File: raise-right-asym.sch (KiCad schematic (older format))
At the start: 105 parts, among them IC1 ATTINY88-A, J1 USB_C_Receptacle_16pin, P1 CONN_01X01, P2 CONN_01X01, P3 CONN_01X01, P4 CONN_01X01, P8 CONN_02X03, Q1 PMOS, -3.6A, 0.02R, SW1 kailh hot plug sockets, SW10 kailh hot plug sockets, SW11 kailh hot plug sockets, SW12 kailh hot plug sockets, SW13 kailh hot plug sockets, SW14 kailh hot plug sockets, SW15 kailh hot plug sockets, SW17 kailh hot plug sockets, SW18 kailh hot plug sockets, SW19 kailh hot plug sockets, SW2 kailh hot plug sockets, SW20 kailh hot plug sockets, SW21 kailh hot plug sockets, SW22 kailh hot plug sockets, SW23 kailh hot plug sockets, SW24 kailh hot plug sockets, SW25 kailh hot plug sockets, SW26 kailh hot plug sockets, SW27 kailh hot plug sockets, SW28 kailh hot plug sockets, SW29 kailh hot plug sockets, SW3 kailh hot plug sockets, SW30 kailh hot plug sockets, SW31 kailh hot plug sockets, SW32 kailh hot plug sockets, SW33 kailh hot plug sockets, SW34 kailh hot plug sockets, SW4 kailh hot plug sockets, SW5 kailh hot plug sockets, SW6 kailh hot plug sockets, SW7 kailh hot plug sockets, SW9 kailh hot plug sockets, T1 CONN_01X01, T2 CONN_01X01, T3 CONN_01X01, U1 ss39et

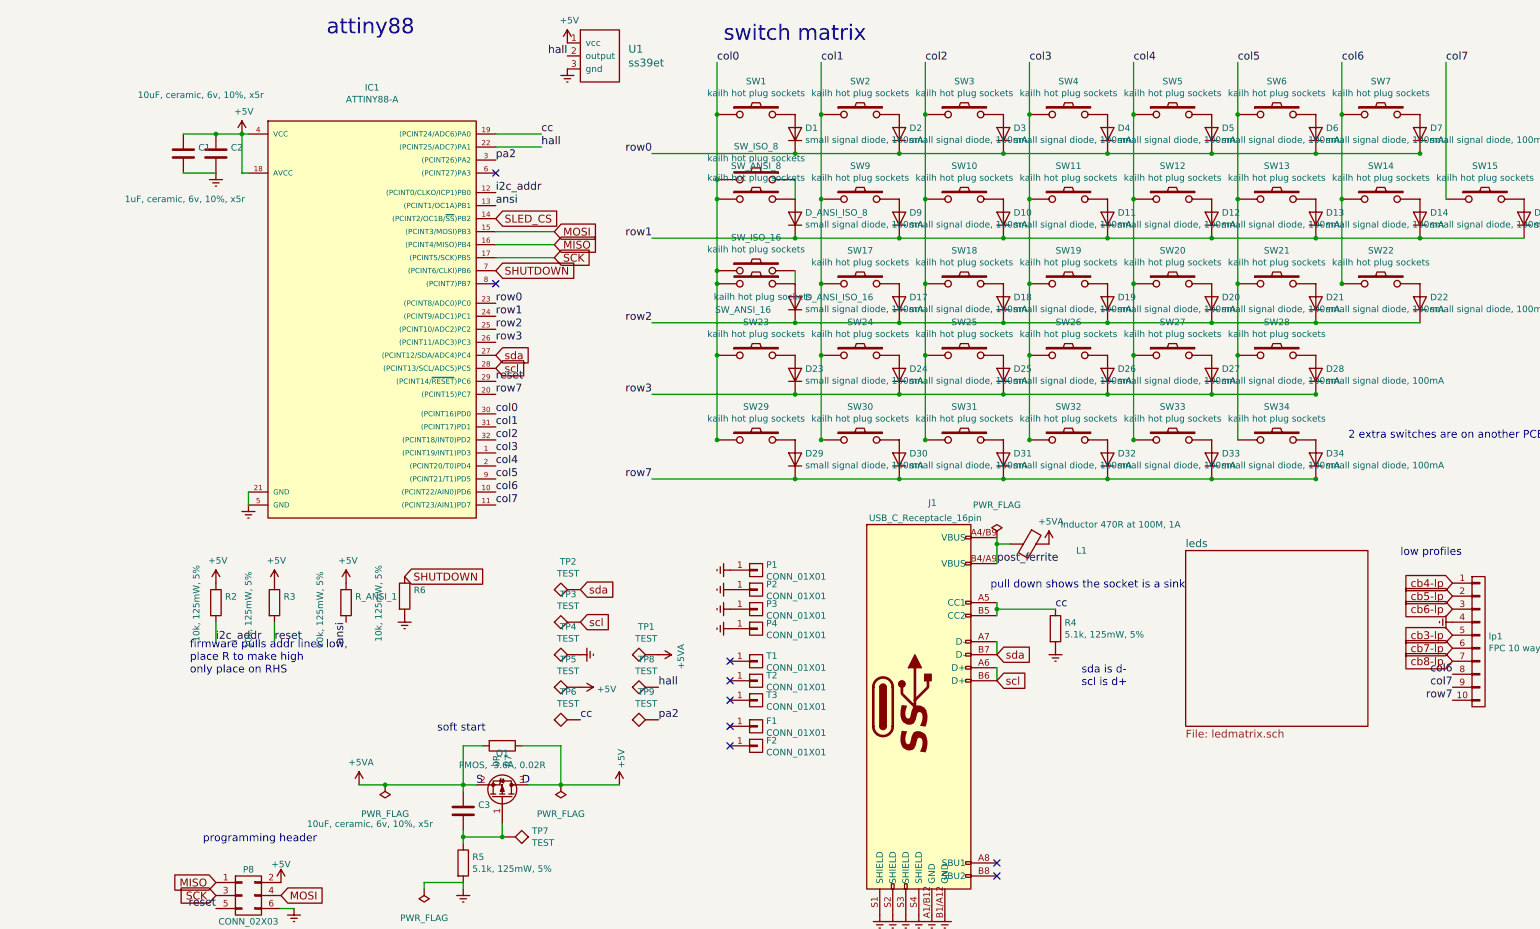
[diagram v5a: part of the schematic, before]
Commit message: 100pf on input, 10uf bypass cap for hall and avcc, testpoints for switches
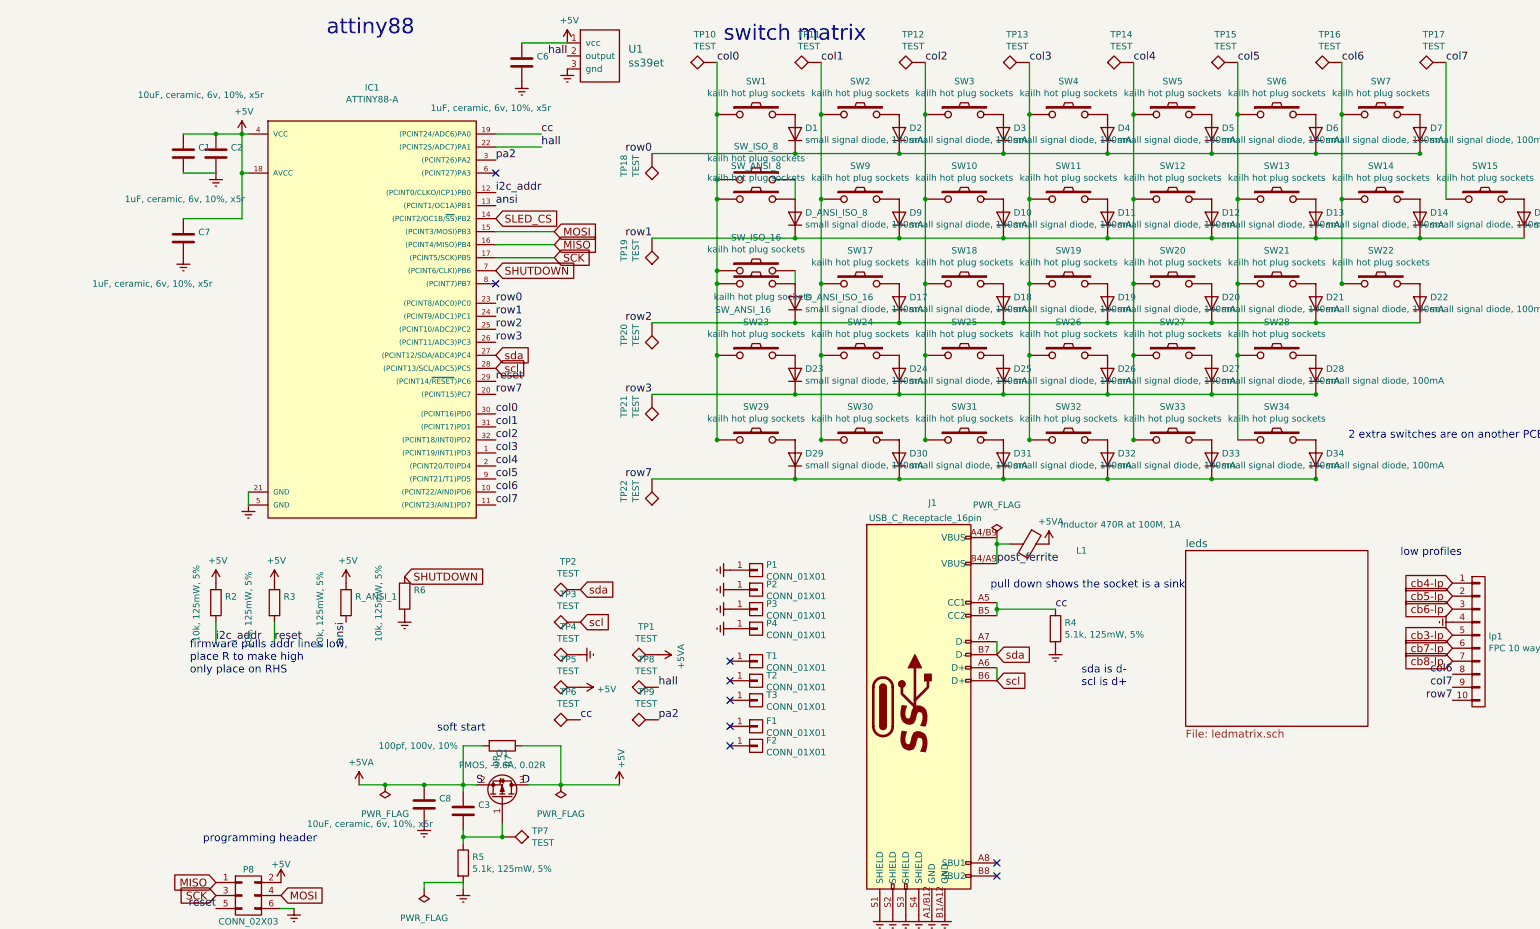
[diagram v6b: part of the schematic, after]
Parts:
- added C6, C7: 1uF, ceramic, 6v, 10%, x5r, raise_fp:C_0603, symbol C
- added C8: 100pf, 100v, 10%, raise_fp:C_0603, symbol C
- added TP10, TP11, TP12, TP13, TP14, TP15, TP16, TP17, TP18, TP19, TP20, TP21, TP22: TEST, raise_fp:Measurement_Point_Round-SMD-Pad_Small, symbol TEST
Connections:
- net +5V: now also C6.1, C7.1
- net +5VA: now also C8.1
- net Earth: now also C6.2, C7.2, C8.2
- net col0: now also TP10.1
- net col1: now also TP11.1
- net col2: now also TP12.1
- net col3: now also TP13.1
- net col4: now also TP14.1
- net col5: now also TP15.1
- net col6: now also TP16.1
- net col7: now also TP17.1
- net row0: now also TP18.1
- net row1: now also TP19.1
- net row2: now also TP20.1
- net row3: now also TP21.1
- net row7: now also TP22.1
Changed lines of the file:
@@
 LIBS:test-jig
 LIBS:usb_c_16pin
-LIBS:Device
 EELAYER 26 0
 EELAYER END
@@
 	1150 1900 1100 1900
 Wire Wire Line
-	1100 1900 1100 1600
+	1100 1600 1100 2250
 Text GLabel 10400 5450 0    60   Input ~ 0
 cb3-lp
+$Comp
+L C C8
+U 1 1 5BEDC1A2
+P 2500 6750
+F 0 "C8" H 2615 6796 50  0000 L CNN
+F 1 "100pf, 100v, 10%" H 2150 7200 50  0000 L CNN
+F 2 "raise_fp:C_0603" H 2538 6600 50  0001 C CNN
+F 3 "" H 2500 6750 50  0000 C CNN
+F 4 "2821263" H 2500 6750 60  0001 C CNN "farnell #"
+F 5 "any/open" H 1850 5000 60  0001 C CNN "supplier"
+F 6 "Value" H 2500 6750 60  0001 C CNN "supplier PN"
+F 7 "Value" H 2500 6750 60  0001 C CNN "MOQ"
+F 8 "Value" H 2500 6750 60  0001 C CNN "leadtime"
+	1    2500 6750
+	1    0    0    -1
+$EndComp
+$Comp
+L Earth #PWR016
+U 1 1 5BEDC459
+P 2500 6900
+F 0 "#PWR016" H 2500 6650 50  0001 C CNN
+F 1 "Earth" H 2500 6750 50  0001 C CNN
+F 2 "" H 2500 6900 50  0000 C CNN
+F 3 "" H 2500 6900 50  0000 C CNN
+	1    2500 6900
+	1    0    0    -1
+$EndComp
+Connection ~ 2500 6600
+$Comp
+L TEST TP22
+U 1 1 5BEDCC0B
+P 4250 4250
+F 0 "TP22" V 4465 4344 50  0000 C CNN
+F 1 "TEST" V 4374 4344 50  0000 C CNN
+F 2 "raise_fp:Measurement_Point_Round-SMD-Pad_Small" H 4250 4250 50  0001 C CNN
+F 3 "" H 4250 4250 50  0001 C CNN
+F 4 "dnp" H 4850 4750 60  0001 C CNN "supplier"
+	1    4250 4250
+	-1   0    0    1
+$EndComp
+$Comp
+L TEST TP21
+U 1 1 5BEDCE9E
+P 4250 3600
+F 0 "TP21" V 4465 3694 50  0000 C CNN
+F 1 "TEST" V 4374 3694 50  0000 C CNN
+F 2 "raise_fp:Measurement_Point_Round-SMD-Pad_Small" H 4250 3600 50  0001 C CNN
+F 3 "" H 4250 3600 50  0001 C CNN
+F 4 "dnp" H 4850 4100 60  0001 C CNN "supplier"
+	1    4250 3600
+	-1   0    0    1
+$EndComp
+$Comp
+L TEST TP20
+U 1 1 5BEDCFA6
+P 4250 3050
+F 0 "TP20" V 4465 3144 50  0000 C CNN
+F 1 "TEST" V 4374 3144 50  0000 C CNN
+F 2 "raise_fp:Measurement_Point_Round-SMD-Pad_Small" H 4250 3050 50  0001 C CNN
+F 3 "" H 4250 3050 50  0001 C CNN
+F 4 "dnp" H 4850 3550 60  0001 C CNN "supplier"
+	1    4250 3050
+	-1   0    0    1
+$EndComp
+$Comp
+L TEST TP19
+U 1 1 5BEDD0A8
+P 4250 2400
+F 0 "TP19" V 4465 2494 50  0000 C CNN
+F 1 "TEST" V 4374 2494 50  0000 C CNN
+F 2 "raise_fp:Measurement_Point_Round-SMD-Pad_Small" H 4250 2400 50  0001 C CNN
+F 3 "" H 4250 2400 50  0001 C CNN
+F 4 "dnp" H 4850 2900 60  0001 C CNN "supplier"
+	1    4250 2400
+	-1   0    0    1
+$EndComp
+$Comp
+L TEST TP18
+U 1 1 5BEDD4B4
+P 4250 1750
+F 0 "TP18" V 4465 1844 50  0000 C CNN
+F 1 "TEST" V 4374 1844 50  0000 C CNN
+F 2 "raise_fp:Measurement_Point_Round-SMD-Pad_Small" H 4250 1750 50  0001 C CNN
+F 3 "" H 4250 1750 50  0001 C CNN
+F 4 "dnp" H 4850 2250 60  0001 C CNN "supplier"
+	1    4250 1750
+	-1   0    0    1
+$EndComp
+$Comp
+L TEST TP10
+U 1 1 5BEDD5BE
+P 4750 1050
+F 0 "TP10" V 4965 1144 50  0000 C CNN
+F 1 "TEST" V 4874 1144 50  0000 C CNN
+F 2 "raise_fp:Measurement_Point_Round-SMD-Pad_Small" H 4750 1050 50  0001 C CNN
+F 3 "" H 4750 1050 50  0001 C CNN
+F 4 "dnp" H 5350 1550 60  0001 C CNN "supplier"
+	1    4750 1050
+	0    -1   -1   0
+$EndComp
+$Comp
+L TEST TP11
+U 1 1 5BEDD76C
+P 5550 1050
+F 0 "TP11" V 5765 1144 50  0000 C CNN
+F 1 "TEST" V 5674 1144 50  0000 C CNN
+F 2 "raise_fp:Measurement_Point_Round-SMD-Pad_Small" H 5550 1050 50  0001 C CNN
+F 3 "" H 5550 1050 50  0001 C CNN
+F 4 "dnp" H 6150 1550 60  0001 C CNN "supplier"
+	1    5550 1050
+	0    -1   -1   0
+$EndComp
+$Comp
+L TEST TP12
+U 1 1 5BEDD884
+P 6350 1050
+F 0 "TP12" V 6565 1144 50  0000 C CNN
+F 1 "TEST" V 6474 1144 50  0000 C CNN
+F 2 "raise_fp:Measurement_Point_Round-SMD-Pad_Small" H 6350 1050 50  0001 C CNN
+F 3 "" H 6350 1050 50  0001 C CNN
+F 4 "dnp" H 6950 1550 60  0001 C CNN "supplier"
+	1    6350 1050
+	0    -1   -1   0
+$EndComp
+$Comp
+L TEST TP13
+U 1 1 5BEDD99E
+P 7150 1050
+F 0 "TP13" V 7365 1144 50  0000 C CNN
+F 1 "TEST" V 7274 1144 50  0000 C CNN
+F 2 "raise_fp:Measurement_Point_Round-SMD-Pad_Small" H 7150 1050 50  0001 C CNN
+F 3 "" H 7150 1050 50  0001 C CNN
+F 4 "dnp" H 7750 1550 60  0001 C CNN "supplier"
+	1    7150 1050
+	0    -1   -1   0
+$EndComp
+$Comp
+L TEST TP14
+U 1 1 5BEDDAB6
+P 7950 1050
+F 0 "TP14" V 8165 1144 50  0000 C CNN
+F 1 "TEST" V 8074 1144 50  0000 C CNN
+F 2 "raise_fp:Measurement_Point_Round-SMD-Pad_Small" H 7950 1050 50  0001 C CNN
+F 3 "" H 7950 1050 50  0001 C CNN
+F 4 "dnp" H 8550 1550 60  0001 C CNN "supplier"
+	1    7950 1050
+	0    -1   -1   0
+$EndComp
+$Comp
+L TEST TP15
+U 1 1 5BEDDFE4
+P 8750 1050
+F 0 "TP15" V 8965 1144 50  0000 C CNN
+F 1 "TEST" V 8874 1144 50  0000 C CNN
+F 2 "raise_fp:Measurement_Point_Round-SMD-Pad_Small" H 8750 1050 50  0001 C CNN
+F 3 "" H 8750 1050 50  0001 C CNN
+F 4 "dnp" H 9350 1550 60  0001 C CNN "supplier"
+	1    8750 1050
+	0    -1   -1   0
+$EndComp
+$Comp
+L TEST TP16
+U 1 1 5BEDE0FE
+P 9550 1050
+F 0 "TP16" V 9765 1144 50  0000 C CNN
+F 1 "TEST" V 9674 1144 50  0000 C CNN
+F 2 "raise_fp:Measurement_Point_Round-SMD-Pad_Small" H 9550 1050 50  0001 C CNN
+F 3 "" H 9550 1050 50  0001 C CNN
+F 4 "dnp" H 10150 1550 60  0001 C CNN "supplier"
+	1    9550 1050
+	0    -1   -1   0
+$EndComp
+$Comp
+L TEST TP17
+U 1 1 5BEDE21E
+P 10350 1050
+F 0 "TP17" V 10565 1144 50  0000 C CNN
+F 1 "TEST" V 10474 1144 50  0000 C CNN
+F 2 "raise_fp:Measurement_Point_Round-SMD-Pad_Small" H 10350 1050 50  0001 C CNN
+F 3 "" H 10350 1050 50  0001 C CNN
+F 4 "dnp" H 10950 1550 60  0001 C CNN "supplier"
+	1    10350 1050
+	0    -1   -1   0
+$EndComp
+$Comp
+L C C7
+U 1 1 5BEDEA06
+P 650 2400
+F 0 "C7" H 765 2446 50  0000 L CNN
+F 1 "1uF, ceramic, 6v, 10%, x5r" H -50 2050 50  0000 L CNN
+F 2 "raise_fp:C_0603" H 688 2250 50  0001 C CNN
+F 3 "" H 650 2400 50  0000 C CNN
+F 4 "1865556" H 650 2400 60  0001 C CNN "farnell #"
+F 5 "any/open" H -250 650 60  0001 C CNN "supplier"
+	1    650  2400
+	1    0    0    -1
+$EndComp
+$Comp
+L Earth #PWR038
+U 1 1 5BEDEB4C
+P 650 2550
+F 0 "#PWR038" H 650 2300 50  0001 C CNN
+F 1 "Earth" H 650 2400 50  0001 C CNN
+F 2 "" H 650 2550 50  0000 C CNN
+F 3 "" H 650 2550 50  0000 C CNN
+	1    650  2550
+	1    0    0    -1
+$EndComp
+Wire Wire Line
+	1100 2250 650  2250
+Connection ~ 1100 1900
+$Comp
+L C C6
+U 1 1 5BEDF086
+P 3250 1050
+F 0 "C6" H 3365 1096 50  0000 L CNN
+F 1 "1uF, ceramic, 6v, 10%, x5r" H 2550 700 50  0000 L CNN
+F 2 "raise_fp:C_0603" H 3288 900 50  0001 C CNN
+F 3 "" H 3250 1050 50  0000 C CNN
+F 4 "1865556" H 3250 1050 60  0001 C CNN "farnell #"
+F 5 "any/open" H 2350 -700 60  0001 C CNN "supplier"
+	1    3250 1050
+	1    0    0    -1
+$EndComp
+$Comp
+L Earth #PWR039
+U 1 1 5BEDF1C2
+P 3250 1200
+F 0 "#PWR039" H 3250 950 50  0001 C CNN
+F 1 "Earth" H 3250 1050 50  0001 C CNN
+F 2 "" H 3250 1200 50  0000 C CNN
+F 3 "" H 3250 1200 50  0000 C CNN
+	1    3250 1200
+	1    0    0    -1
+$EndComp
+Wire Wire Line
+	3250 900  3600 900
 $EndSCHEMATC

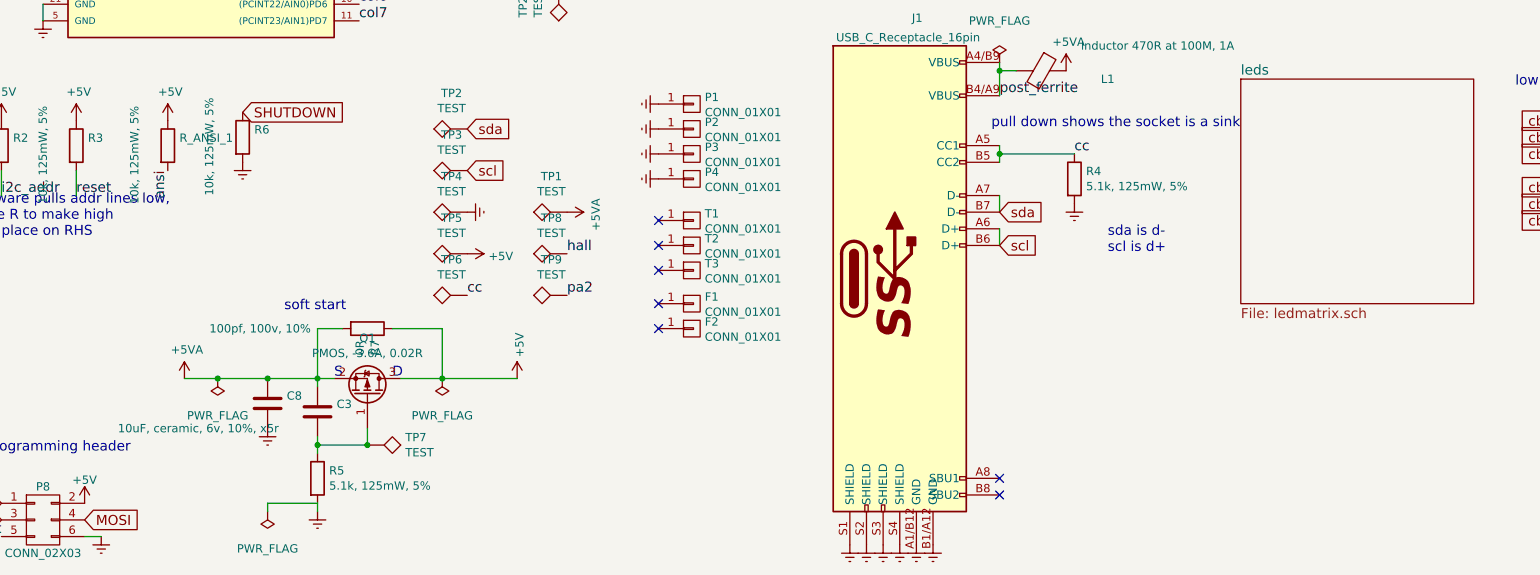
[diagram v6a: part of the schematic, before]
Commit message: holes to 4mm, sled testpoints, usbC mask on locator points, diode and cap fp improvements
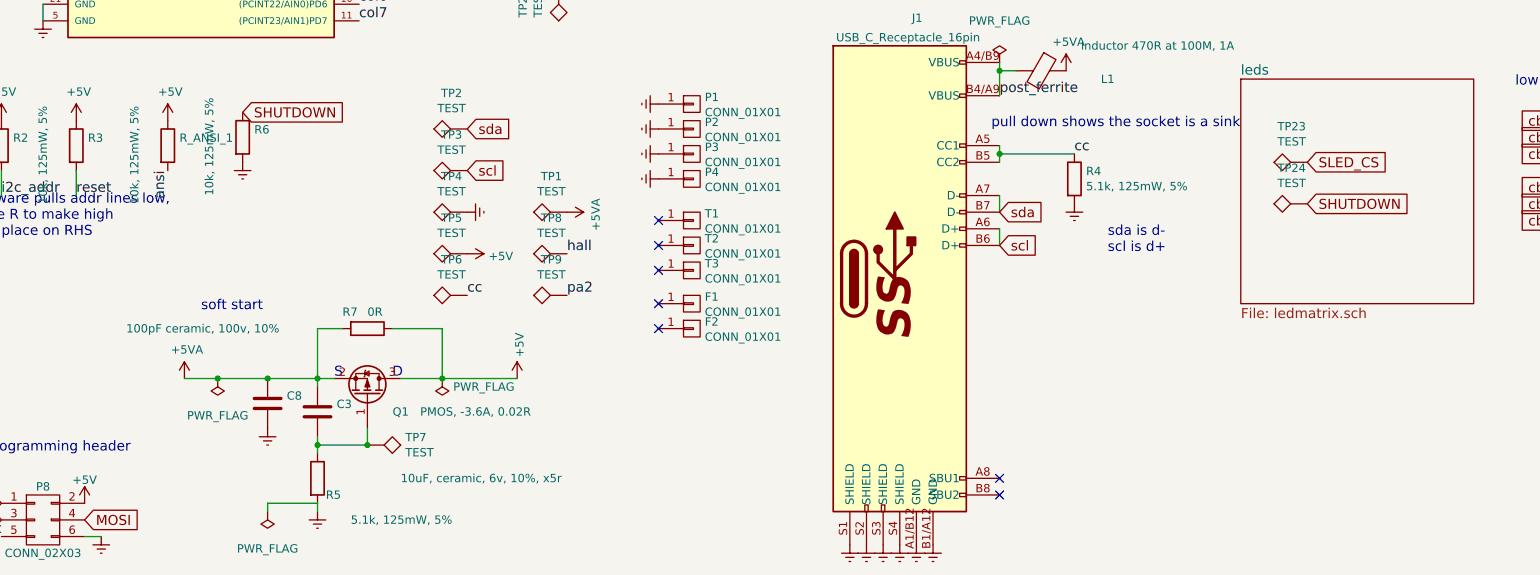
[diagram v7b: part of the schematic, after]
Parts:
- added TP23, TP24: TEST, raise_fp:Measurement_Point_Round-SMD-Pad_Small, symbol TEST
- C8: value 100pf, 100v, 10% -> 100pF ceramic, 100v, 10%
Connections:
- net SHUTDOWN: now also TP24.1
- net SLED_CS: now also TP23.1
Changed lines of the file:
@@
 P 2800 6800
 F 0 "C3" H 2915 6846 50  0000 L CNN
-F 1 "10uF, ceramic, 6v, 10%, x5r" H 1600 6700 50  0000 L CNN
+F 1 "10uF, ceramic, 6v, 10%, x5r" H 3300 6400 50  0000 L CNN
 F 2 "raise_fp:C_0603" H 2838 6650 50  0001 C CNN
 F 3 "" H 2800 6800 50  0000 C CNN
@@
 U 1 1 59D15DC4
 P 2800 7200
-F 0 "R5" H 2870 7246 50  0000 L CNN
-F 1 "5.1k, 125mW, 5%" H 2870 7155 50  0000 L CNN
+F 0 "R5" H 2850 7100 50  0000 L CNN
+F 1 "5.1k, 125mW, 5%" H 3000 6950 50  0000 L CNN
 F 2 "raise_fp:R_0603" V 2730 7200 50  0001 C CNN
 F 3 "" H 2800 7200 50  0000 C CNN
@@
 	1    0    0    -1
 $EndComp
-Text Notes 2600 6200 0    60   ~ 0
+Text Notes 2100 6200 0    60   ~ 0
 soft start
 $Comp
@@
 P 3550 6600
 F 0 "#FLG03" H 3550 6695 50  0001 C CNN
-F 1 "PWR_FLAG" H 3550 6823 50  0000 C CNN
+F 1 "PWR_FLAG" H 3300 6650 50  0000 C CNN
 F 2 "" H 3550 6600 50  0000 C CNN
 F 3 "" H 3550 6600 50  0000 C CNN
@@
 	1    0    0    -1
 $EndComp
-$Sheet
-S 8350 4800 1400 1350
-U 59D12F0F
-F0 "leds" 60
-F1 "ledmatrix.sch" 60
-$EndSheet
 $Comp
 L SW_PUSH SW14
@@
 U 1 1 5A315925
 P 3100 6700
-F 0 "Q1" V 3443 6700 50  0000 C CNN
-F 1 "PMOS, -3.6A, 0.02R" V 3352 6700 50  0000 C CNN
+F 0 "Q1" V 3000 6900 50  0000 C CNN
+F 1 "PMOS, -3.6A, 0.02R" V 3000 7350 50  0000 C CNN
 F 2 "raise_fp:SOT-23" H 3300 6800 50  0001 C CNN
 F 3 "" H 3100 6700 50  0001 C CNN
@@
 U 1 1 5B2B6980
 P 3100 6300
-F 0 "R7" H 3170 6346 50  0000 L CNN
-F 1 "0R" H 3170 6255 50  0000 L CNN
+F 0 "R7" V 3000 6150 50  0000 L CNN
+F 1 "0R" V 3000 6300 50  0000 L CNN
 F 2 "raise_fp:R_0603" V 3030 6300 50  0001 C CNN
 F 3 "" H 3100 6300 50  0000 C CNN
@@
 P 2500 6750
 F 0 "C8" H 2615 6796 50  0000 L CNN
-F 1 "100pf, 100v, 10%" H 2150 7200 50  0000 L CNN
+F 1 "100pF ceramic, 100v, 10%" H 1650 7200 50  0000 L CNN
 F 2 "raise_fp:C_0603" H 2538 6600 50  0001 C CNN
 F 3 "" H 2500 6750 50  0000 C CNN
@@
 Wire Wire Line
 	3250 900  3600 900
+$Comp
+L TEST TP23
+U 1 1 5C12D3B2
+P 8750 5300
+F 0 "TP23" V 8965 5394 50  0000 C CNN
+F 1 "TEST" V 8874 5394 50  0000 C CNN
+F 2 "raise_fp:Measurement_Point_Round-SMD-Pad_Small" H 8750 5300 50  0001 C CNN
+F 3 "" H 8750 5300 50  0001 C CNN
+F 4 "dnp" H 4450 -550 60  0001 C CNN "supplier"
+	1    8750 5300
+	0    -1   -1   0
+$EndComp
+$Comp
+L TEST TP24
+U 1 1 5C12D3BA
+P 8750 5550
+F 0 "TP24" V 8965 5644 50  0000 C CNN
+F 1 "TEST" V 8874 5644 50  0000 C CNN
+F 2 "raise_fp:Measurement_Point_Round-SMD-Pad_Small" H 8750 5550 50  0001 C CNN
+F 3 "" H 8750 5550 50  0001 C CNN
+F 4 "dnp" H 4450 -550 60  0001 C CNN "supplier"
+	1    8750 5550
+	0    -1   -1   0
+$EndComp
+Text GLabel 8750 5550 2    60   Input ~ 0
+SHUTDOWN
+Text GLabel 8750 5300 2    60   Input ~ 0
+SLED_CS
+$Sheet
+S 8350 4800 1400 1350
+U 59D12F0F
+F0 "leds" 60
+F1 "ledmatrix.sch" 60
+$EndSheet
 $EndSCHEMATC
